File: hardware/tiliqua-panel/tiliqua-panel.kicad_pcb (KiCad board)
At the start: 2 copper layers, 30 x 128.5 mm, 13 parts

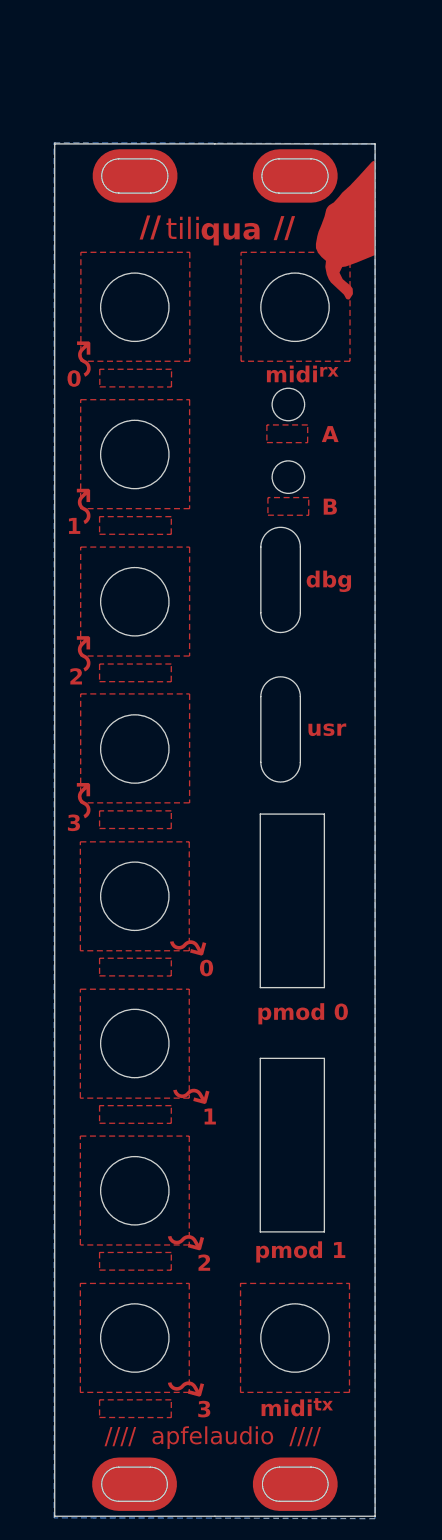
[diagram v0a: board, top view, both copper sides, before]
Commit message: hardware/r2: squash in all changes for tiliqua R2 (#17)
* squash in all changes for Tiliqua R2
* add schematics for all components of Tiliqua R2
* update README and add lightbox photos
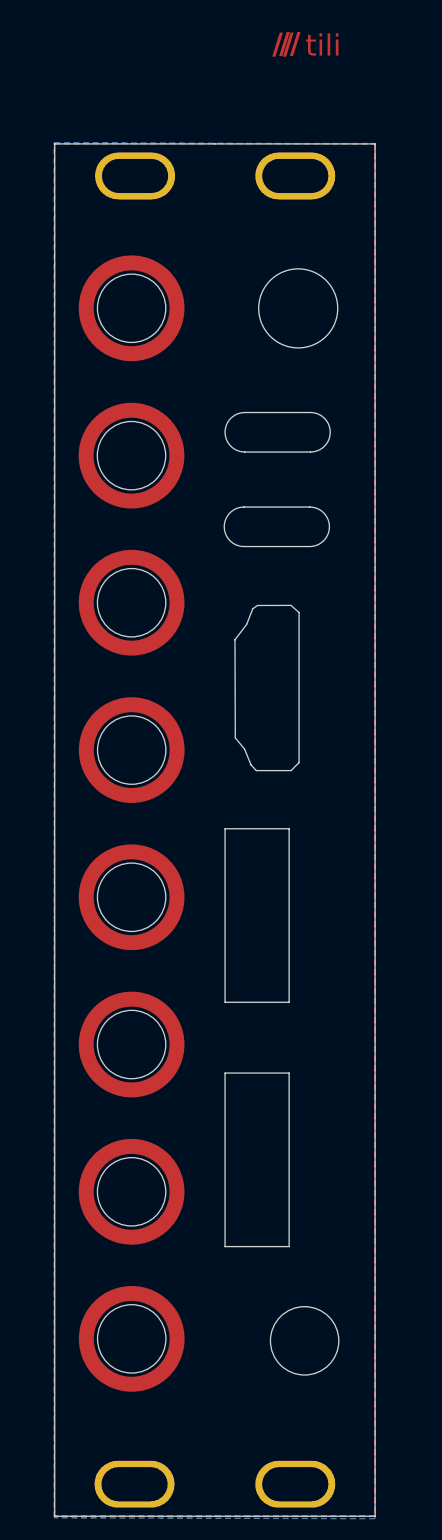
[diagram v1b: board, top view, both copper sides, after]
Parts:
- removed the REF** at (19.5, 15.3)
- removed the REF** at (4.50, 70.4)
- removed the REF** at (4.50, 29.1)
- removed the REF** at (4.50, 84.2)
- removed the REF** at (4.50, 42.9)
- removed the REF** at (4.50, 98.0)
- removed the REF** at (4.50, 56.7)
- removed the REF** at (4.50, 111.8)
- added E1: MountingHole_Pad, , F.Cu at (4.53, 3.00)
- added E2: MountingHole_Pad, , F.Cu at (19.5, 3.00)
- added E3: MountingHole_Pad, , F.Cu at (4.47, 125.5)
- added E4: MountingHole_Pad, , F.Cu at (19.5, 125.5)
- added REF**: MountingHole_6.4mm_M6, MountingHole:MountingHole_6.4mm_M6, F.Cu at (4.21, 111.9)
- added REF**: MountingHole_7.4mm_M6, MountingHole:MountingHole_6.4mm_M6, F.Cu at (19.8, 15.4)
- added REF**: MountingHole_6.4mm_M6, MountingHole:MountingHole_6.4mm_M6, F.Cu at (4.20, 84.3)
- added REF**: MountingHole_6.4mm_M6, MountingHole:MountingHole_6.4mm_M6, F.Cu at (4.20, 70.5)
- added REF**: MountingHole_6.4mm_M6, MountingHole:MountingHole_6.4mm_M6, F.Cu at (4.20, 43.0)
- added REF**: MountingHole_6.4mm_M6, MountingHole:MountingHole_6.4mm_M6, F.Cu at (4.20, 98.1)
- added REF**: MountingHole_6.4mm_M6, MountingHole:MountingHole_6.4mm_M6, F.Cu at (4.19, 29.2)
- added REF**: MountingHole_6.4mm_M6, MountingHole:MountingHole_6.4mm_M6, F.Cu at (4.21, 56.8)
- moved G*** 65.6 mm to (25.8, 73.1), turned to 0 degrees
- moved REF** 3.32 mm to (11.7, 9.50)
- moved REF** 0.94 mm to (20.4, 112.1)
- moved REF** 0.83 mm to (-0.80, 8.88)
- moved REF** 0.32 mm to (4.20, 15.4)
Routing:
- added copper zone on B.Cu, net GND
- added copper zone on F.Cu, net GND
- removed copper zone on B.Cu, net (none)
- removed copper zone on F.Cu, net (none)
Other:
- outline, holes or cut-outs redrawn
- board text added: "[apfelaudio]"
- board text added: "[tiliqua]"
- board text added: "dvi"
- board text added: "ex0"
- board text added: "ex1"
- board text added: "tiliqua"
- board text added: "usb2"
- board text removed: "//// apfelaudio ////"
- board text removed: "A"
- board text removed: "B"
- board text removed: "midi^{tx}"
- board text removed: "pmod 0"
- board text removed: "pmod 1"
- board text removed: "usr"

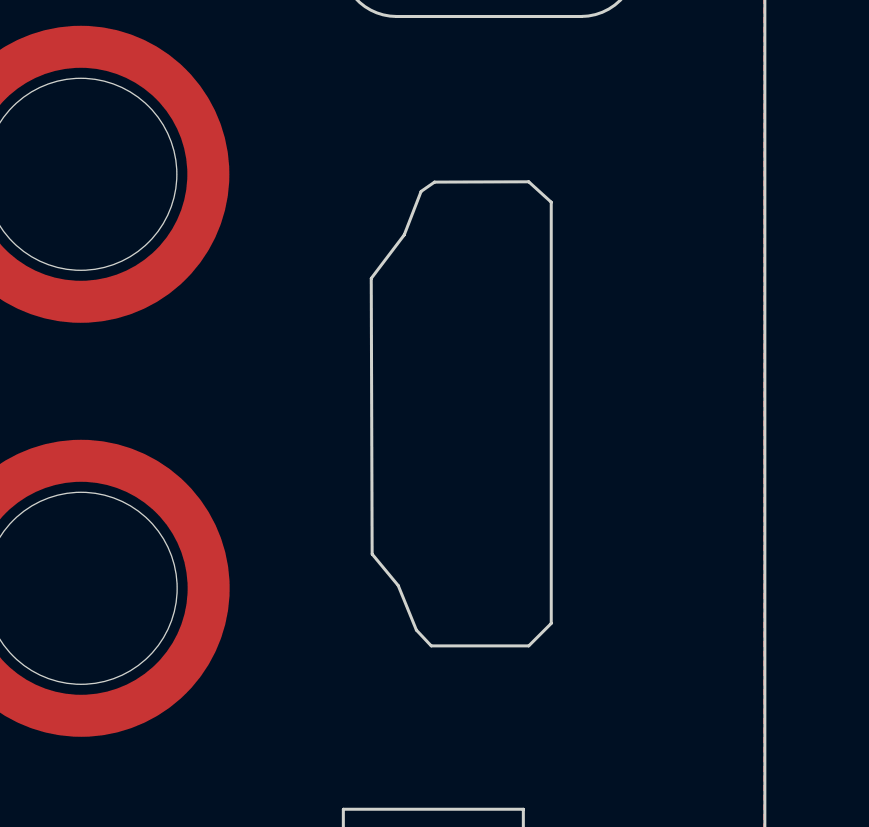
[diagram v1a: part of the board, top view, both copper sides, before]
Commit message: hw/panel-r3: adjust DVI connector cutout
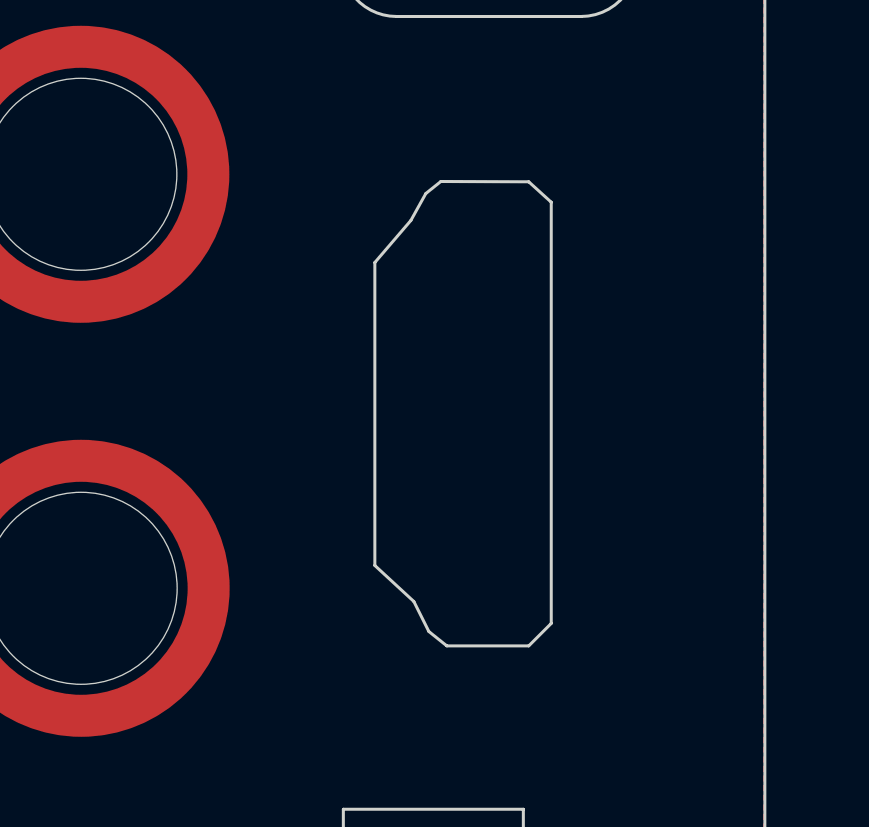
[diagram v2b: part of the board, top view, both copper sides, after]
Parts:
- moved REF** 0.40 mm to (12.1, 9.50)
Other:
- outline, holes or cut-outs redrawn
